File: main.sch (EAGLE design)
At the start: 8 parts

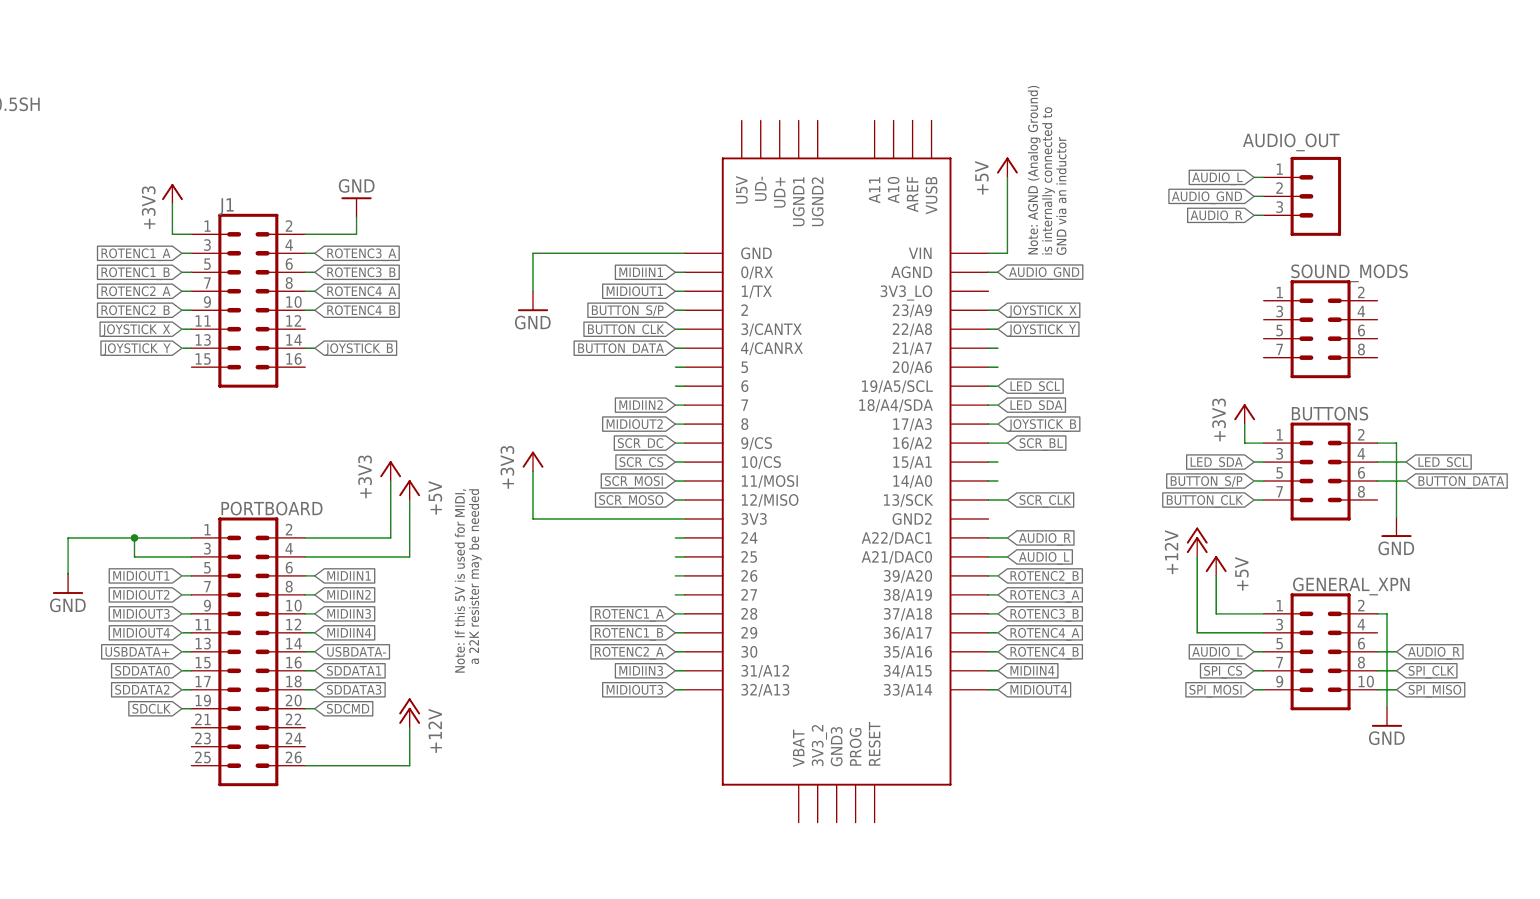
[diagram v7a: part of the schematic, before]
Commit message: KNOBBOARD pinout fixed, seperate audio ground added, pinhead lib switched to, pcb rerouted. TODO general expansion and mixing
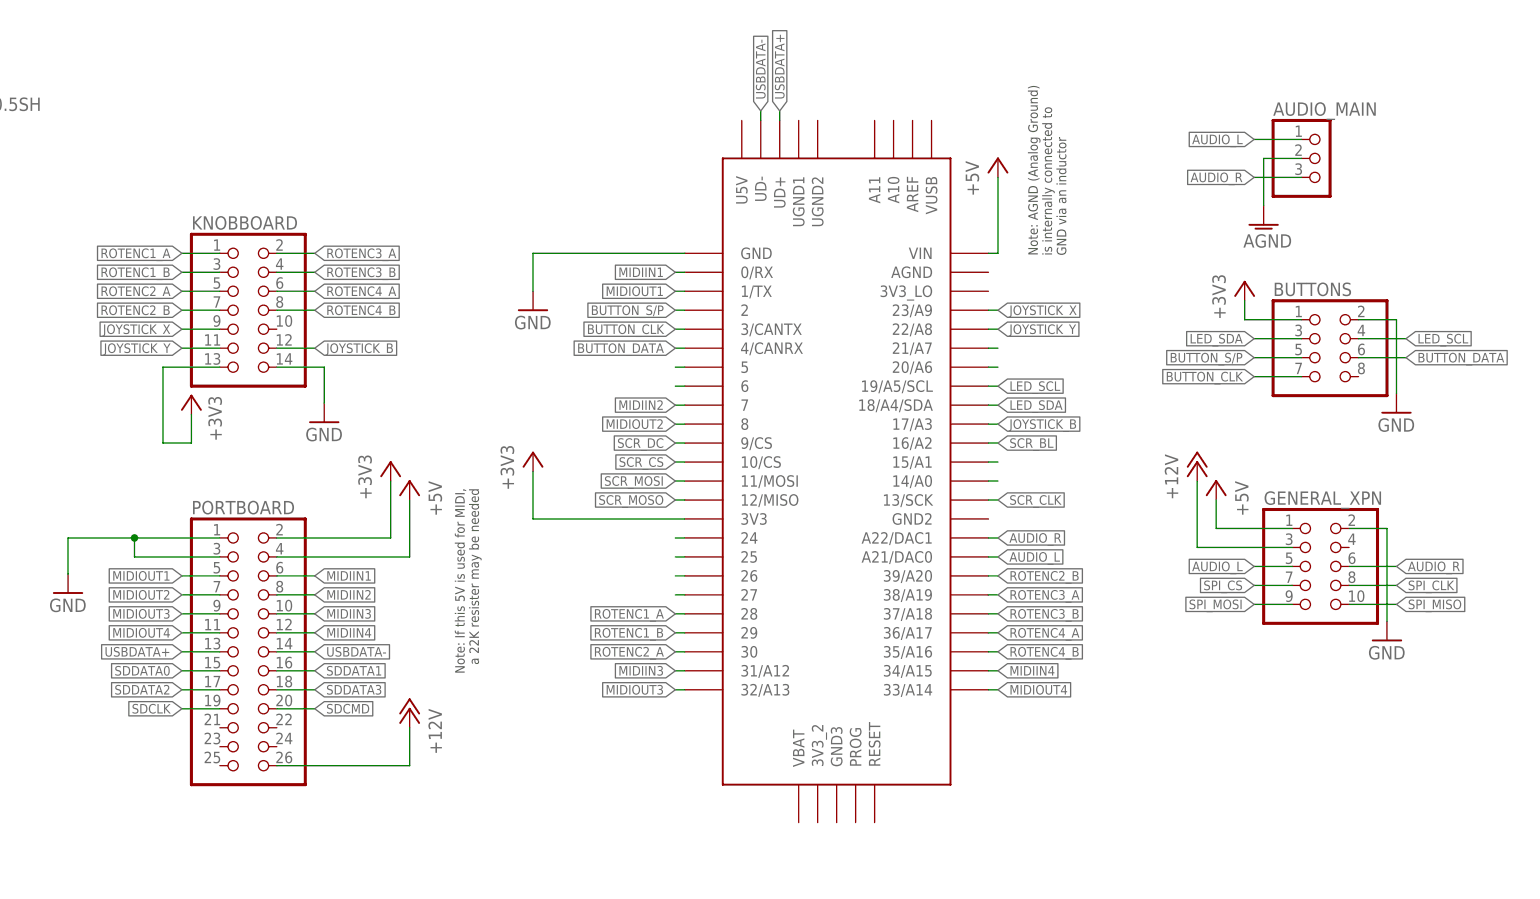
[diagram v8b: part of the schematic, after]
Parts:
- removed AUDIO_OUT: (no value), SparkFun-Connectors:CONN_03
- removed J1: (no value), SparkFun-Connectors:CONN_08X2
- removed SOUND_MODS: (no value), SparkFun-Connectors:CONN_04X2
- added AUDIO_MAIN: (no value), pinhead:PINHD-1X3
- added KNOBBOARD: (no value), pinhead:PINHD-2X7
- BUTTONS: device SparkFun-Connectors:CONN_04X2 -> pinhead:PINHD-2X4
- GENERAL_XPN: device SparkFun-Connectors:CONN_05X2PTH -> pinhead:PINHD-2X5
- PORTBOARD: device SparkFun-Connectors:CONN_13X22X13 -> pinhead:PINHD-2X13
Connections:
- removed net AUDIO_GND: AUDIO_OUT.2, U$1.AGND
- new net AGND: AUDIO_MAIN.2
- net +3V3: now also KNOBBOARD.13; no longer J1.1
- net AUDIO_L: now also AUDIO_MAIN.1; no longer AUDIO_OUT.1
- net AUDIO_R: now also AUDIO_MAIN.3; no longer AUDIO_OUT.3
- net GND: now also KNOBBOARD.14; no longer J1.2
- net JOYSTICK_B: now also KNOBBOARD.12; no longer J1.14
- net JOYSTICK_X: now also KNOBBOARD.9; no longer J1.11
- net JOYSTICK_Y: now also KNOBBOARD.11; no longer J1.13
- net ROTENC1_A: now also KNOBBOARD.1; no longer J1.3
- net ROTENC1_B: now also KNOBBOARD.3; no longer J1.5
- net ROTENC2_A: now also KNOBBOARD.5; no longer J1.7
- net ROTENC2_B: now also KNOBBOARD.7; no longer J1.9
- net ROTENC3_A: now also KNOBBOARD.2; no longer J1.4
- net ROTENC3_B: now also KNOBBOARD.4; no longer J1.6
- net ROTENC4_A: now also KNOBBOARD.6; no longer J1.8
- net ROTENC4_B: now also KNOBBOARD.8; no longer J1.10
- net USBDATA+: now also U$1.UD+
- net USBDATA-: now also U$1.UD-
